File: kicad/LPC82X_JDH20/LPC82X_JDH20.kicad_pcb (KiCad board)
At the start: 2 copper layers, 18.7 x 23.8 mm, 24 parts, among them J1 Conn_01x09, J2 JTAG_2X05, J3 Conn_01x09, U1 LPC824M201JDH20, Y1 12MHz

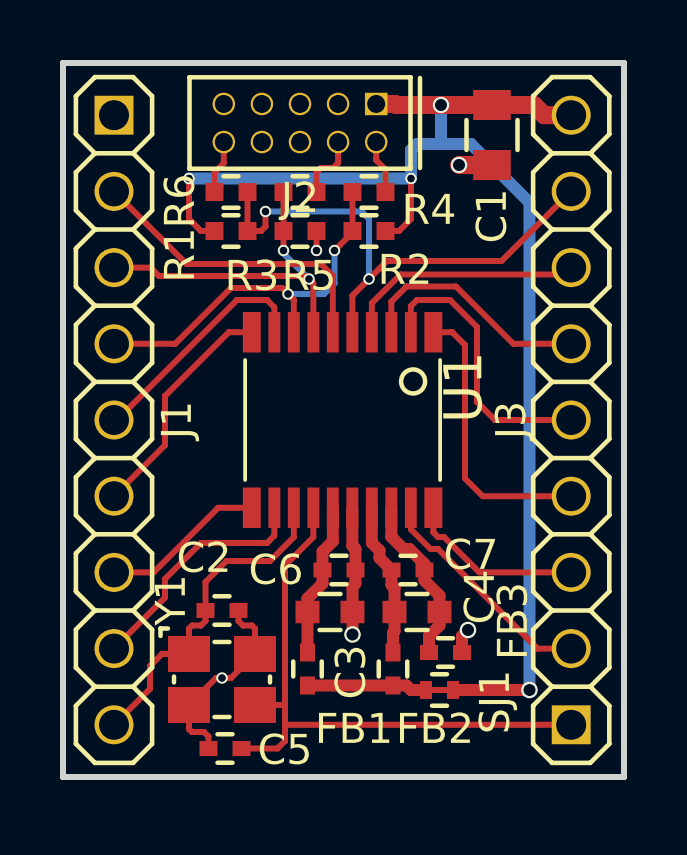
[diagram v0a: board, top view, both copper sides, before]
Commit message: updated a few traces and silk screen bits
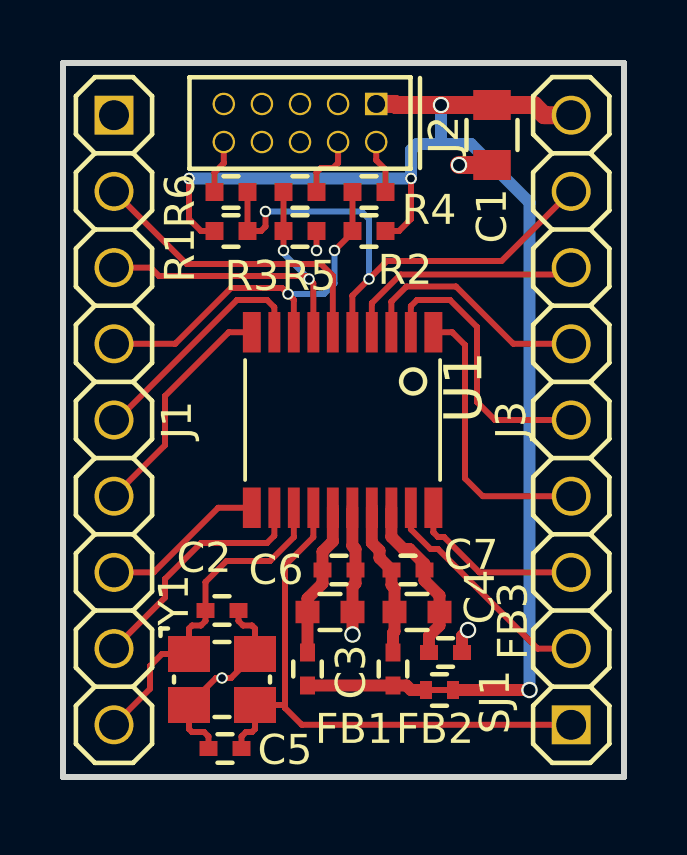
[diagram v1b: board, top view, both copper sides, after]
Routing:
- net /PIO0_8: track 20.3 -> 19.6 mm
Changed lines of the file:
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@@
     (thickness 1.6)
     (drawings 5)
-    (tracks 219)
+    (tracks 221)
     (zones 0)
     (modules 24)
@@
     (visible_elements FFFFFF7F)
     (pcbplotparams
-      (layerselection 0x00030_80000001)
-      (usegerberextensions false)
+      (layerselection 0x010f0_ffffffff)
+      (usegerberextensions true)
       (usegerberattributes false)
       (usegerberadvancedattributes false)
@@
       (outputformat 1)
       (mirror false)
-      (drillshape 1)
+      (drillshape 0)
       (scaleselection 1)
-      (outputdirectory ""))
+      (outputdirectory "LPC82X_JDH20_plots"))
   )
   (net 0 "")
@@
   (module SquantorConnectors:Header-0127-2X05-H006 (layer F.Cu)
     (at 133.2 91.7 180)
-    (fp_text reference J2 (at 0 -2.5 180) (layer F.SilkS)
+    (fp_text reference J2 (at -4.8 -0.4 270) (layer F.SilkS)
       (effects (font (size 1 1) (thickness 0.15)))
     )
@@
     (at 130.6 110.25)
     (attr smd)
-    (fp_text reference Y1 (at -1.7 -2.65 90) (layer F.SilkS)
+    (fp_text reference Y1 (at -1.6 -2.65 90) (layer F.SilkS)
       (effects (font (size 1 1) (thickness 0.15)))
     )
@@
   (segment (start 133.645 104.525) (end 133.645 105.505) (width 0.2) (layer F.Cu) (net 7))
   (segment (start 133.645 105.505) (end 132.7 106.45) (width 0.2) (layer F.Cu) (net 7))
-  (segment (start 132.45 112.55) (end 131.25 112.55) (width 0.2) (layer F.Cu) (net 7))
-  (segment (start 132.7 112.3) (end 132.45 112.55) (width 0.2) (layer F.Cu) (net 7))
-  (segment (start 132.71 111.76) (end 132.7 111.75) (width 0.2) (layer F.Cu) (net 7))
-  (segment (start 142.24 111.76) (end 132.71 111.76) (width 0.2) (layer F.Cu) (net 7))
-  (segment (start 132.7 111.75) (end 132.7 112.3) (width 0.2) (layer F.Cu) (net 7))
   (segment (start 132.65 111.1) (end 132.7 111.15) (width 0.2) (layer F.Cu) (net 7))
   (segment (start 131.7 111.1) (end 132.65 111.1) (width 0.2) (layer F.Cu) (net 7))
   (segment (start 132.7 106.45) (end 132.7 111.15) (width 0.2) (layer F.Cu) (net 7))
-  (segment (start 132.7 111.15) (end 132.7 111.75) (width 0.2) (layer F.Cu) (net 7))
+  (segment (start 131.25 112.55) (end 131.25 112.15) (width 0.2) (layer F.Cu) (net 7))
+  (segment (start 131.25 112.15) (end 131.4 112) (width 0.2) (layer F.Cu) (net 7))
+  (segment (start 131.4 112) (end 131.6 112) (width 0.2) (layer F.Cu) (net 7))
+  (segment (start 131.7 111.9) (end 131.7 111.1) (width 0.2) (layer F.Cu) (net 7))
+  (segment (start 131.6 112) (end 131.7 111.9) (width 0.2) (layer F.Cu) (net 7))
+  (segment (start 132.7 111.2) (end 132.7 111.15) (width 0.2) (layer F.Cu) (net 7))
+  (segment (start 142.24 111.76) (end 133.26 111.76) (width 0.2) (layer F.Cu) (net 7))
+  (segment (start 133.26 111.76) (end 132.7 111.2) (width 0.2) (layer F.Cu) (net 7))
   (segment (start 133.45 110.45) (end 136.3 110.45) (width 0.4) (layer F.Cu) (net 8))
   (segment (start 136.3 110.45) (end 136.75 110.45) (width 0.4) (layer F.Cu) (net 8))

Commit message: updated PCB and plots
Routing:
- net /PIO0_23: track 9.47 -> 7.74 mm
- net /PIO0_17: track 9.42 -> 7.96 mm
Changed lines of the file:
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@@
     (thickness 1.6)
     (drawings 5)
-    (tracks 221)
+    (tracks 218)
     (zones 0)
     (modules 24)
@@
     (at 134.62 101.6 180)
     (descr "<li><b>SOT360</b><hr>\n<ul><li>TSSOP20: plastic thin shrink small outline package; 20 leads; body width 4.4 mm\n<li><u>JEDEC</u>: MO-153\n<li><u>IEC</u>: </ul>")
-    (fp_text reference U1 (at -4.78 -0.1 270) (layer F.SilkS)
-      (effects (font (size 1.27 1.27) (thickness 0.15)) (justify left bottom))
-    )
-    (fp_text value LPC824M201JDH20 (at 5.3 3.6 270) (layer F.Fab)
-      (effects (font (size 1.27 1.27) (thickness 0.15)) (justify left bottom))
+    (fp_text reference U1 (at -3.5 2.2 270) (layer F.SilkS)
+      (effects (font (size 1 1) (thickness 0.15)) (justify left bottom))
+    )
+    (fp_text value LPC824M201JDH20 (at 4.6 3.1 270) (layer F.Fab)
+      (effects (font (size 1 1) (thickness 0.15)) (justify left bottom))
     )
     (fp_line (start -3.25 -2.2) (end 3.25 -2.2) (layer Dwgs.User) (width 0.127))
@@
   (segment (start 128.7 102.44) (end 127 104.14) (width 0.2) (layer F.Cu) (net 13))
   (segment (start 128.7 100.8) (end 128.7 102.44) (width 0.2) (layer F.Cu) (net 13))
-  (segment (start 131.595 104.525) (end 130.475 104.525) (width 0.2) (layer F.Cu) (net 14))
   (segment (start 128.32 106.68) (end 127 106.68) (width 0.2) (layer F.Cu) (net 14))
   (segment (start 130.475 104.525) (end 128.32 106.68) (width 0.2) (layer F.Cu) (net 14))
+  (segment (start 130.475 104.525) (end 131.595 104.525) (width 0.2) (layer F.Cu) (net 14))
   (segment (start 132.345 104.525) (end 132.345 105.455) (width 0.2) (layer F.Cu) (net 15))
   (segment (start 132.345 105.455) (end 132.1 105.7) (width 0.2) (layer F.Cu) (net 15))
@@
   (segment (start 140.31 99.06) (end 142.24 99.06) (width 0.2) (layer F.Cu) (net 21))
   (segment (start 138.4 97.15) (end 140.31 99.06) (width 0.2) (layer F.Cu) (net 21))
+  (segment (start 142.2 101.6) (end 142.24 101.6) (width 0.2) (layer F.Cu) (net 22))
+  (segment (start 138.2 97.6) (end 142.2 101.6) (width 0.2) (layer F.Cu) (net 22))
   (segment (start 136.895 98.675) (end 136.895 97.805) (width 0.2) (layer F.Cu) (net 22))
+  (segment (start 137.1 97.6) (end 138.2 97.6) (width 0.2) (layer F.Cu) (net 22))
   (segment (start 136.895 97.805) (end 137.1 97.6) (width 0.2) (layer F.Cu) (net 22))
-  (segment (start 137.1 97.6) (end 138.2 97.6) (width 0.2) (layer F.Cu) (net 22))
-  (segment (start 138.2 97.6) (end 139.1 98.5) (width 0.2) (layer F.Cu) (net 22))
-  (segment (start 139.1 98.5) (end 139.1 101) (width 0.2) (layer F.Cu) (net 22))
-  (segment (start 139.7 101.6) (end 142.24 101.6) (width 0.2) (layer F.Cu) (net 22))
-  (segment (start 139.1 101) (end 139.7 101.6) (width 0.2) (layer F.Cu) (net 22))
+  (segment (start 138.7 100.6) (end 142.24 104.14) (width 0.2) (layer F.Cu) (net 23))
+  (segment (start 138.7 99.1) (end 138.7 100.6) (width 0.2) (layer F.Cu) (net 23))
   (segment (start 137.645 98.675) (end 138.275 98.675) (width 0.2) (layer F.Cu) (net 23))
   (segment (start 138.275 98.675) (end 138.7 99.1) (width 0.2) (layer F.Cu) (net 23))
-  (segment (start 138.7 99.1) (end 138.7 103.55) (width 0.2) (layer F.Cu) (net 23))
-  (segment (start 139.29 104.14) (end 142.24 104.14) (width 0.2) (layer F.Cu) (net 23))
-  (segment (start 138.7 103.55) (end 139.29 104.14) (width 0.2) (layer F.Cu) (net 23))
   (segment (start 137.645 104.525) (end 137.645 105.345) (width 0.2) (layer F.Cu) (net 24))
   (segment (start 137.645 105.345) (end 137.8 105.5) (width 0.2) (layer F.Cu) (net 24))

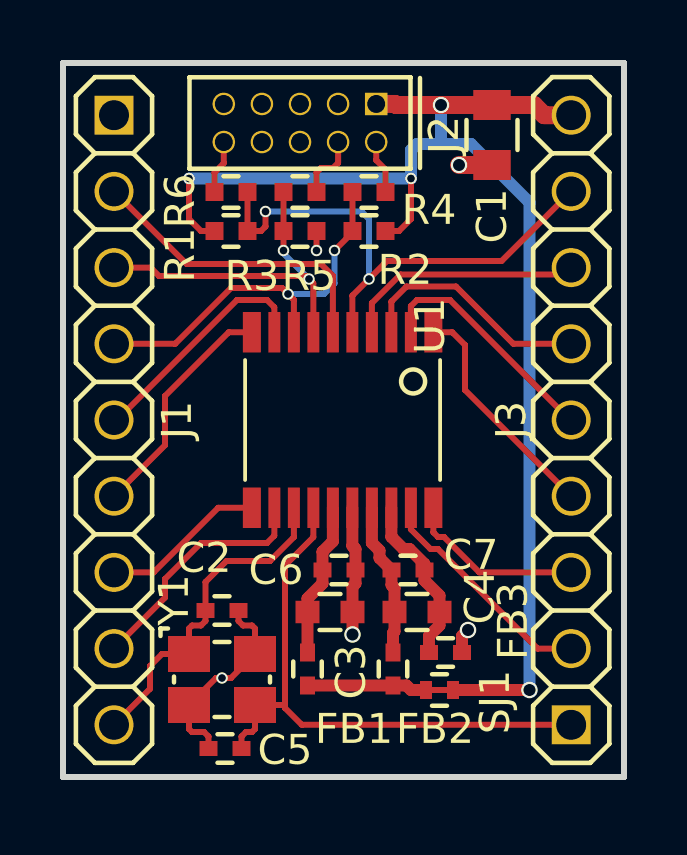
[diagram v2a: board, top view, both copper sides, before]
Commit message: small silk updates, updated values, top groundplane
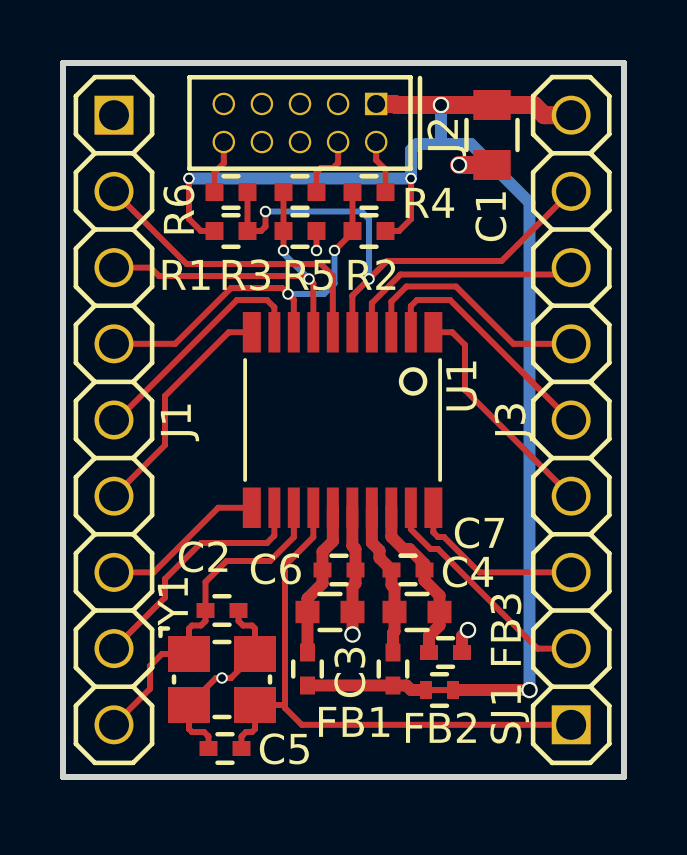
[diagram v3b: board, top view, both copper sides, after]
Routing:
- added copper zone on F.Cu, net VSS
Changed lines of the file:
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@@
     (47 F.CrtYd user)
     (48 B.Fab user)
-    (49 F.Fab user hide)
+    (49 F.Fab user)
   )
   (setup
-    (last_trace_width 0.2)
+    (last_trace_width 0.1524)
     (user_trace_width 0.1524)
     (user_trace_width 0.2)
@@
       (effects (font (size 1 1) (thickness 0.15)))
     )
-    (fp_text value 10u (at 0 2.1 90) (layer F.Fab)
+    (fp_text value 10u (at -2.7 0 90) (layer F.Fab)
       (effects (font (size 1 1) (thickness 0.15)))
     )
@@
       (effects (font (size 1 1) (thickness 0.15)))
     )
-    (fp_text value 18p (at 0 1.7) (layer F.Fab)
+    (fp_text value 18p (at -0.6 -1.75) (layer F.Fab)
       (effects (font (size 1 1) (thickness 0.15)))
     )
@@
       (effects (font (size 1 1) (thickness 0.15)))
     )
-    (fp_text value 1u (at 0 1.9) (layer F.Fab)
+    (fp_text value 1u (at 0.6 2 90) (layer F.Fab)
       (effects (font (size 1 1) (thickness 0.15)))
     )
@@
     (tags "capacitor 0603")
     (attr smd)
-    (fp_text reference C4 (at 2.1 -0.5 90) (layer F.SilkS)
-      (effects (font (size 1 1) (thickness 0.15)))
-    )
-    (fp_text value 1u (at 0 1.9) (layer F.Fab)
+    (fp_text reference C4 (at 1.7 -1.3) (layer F.SilkS)
+      (effects (font (size 1 1) (thickness 0.15)))
+    )
+    (fp_text value 1u (at 1.8 -1.4) (layer F.Fab)
       (effects (font (size 1 1) (thickness 0.15)))
     )
@@
       (effects (font (size 1 1) (thickness 0.15)))
     )
-    (fp_text value 18p (at 0 1.7 180) (layer F.Fab)
+    (fp_text value 18p (at -2 -0.05 180) (layer F.Fab)
       (effects (font (size 1 1) (thickness 0.15)))
     )
@@
       (effects (font (size 1 1) (thickness 0.15)))
     )
-    (fp_text value 100n (at 0 1.7) (layer F.Fab)
+    (fp_text value 100n (at -2 0) (layer F.Fab)
       (effects (font (size 1 1) (thickness 0.15)))
     )
@@
     (tags "capacitor 0402")
     (attr smd)
-    (fp_text reference C7 (at 2.1 -0.5) (layer F.SilkS)
-      (effects (font (size 1 1) (thickness 0.15)))
-    )
-    (fp_text value 100n (at 0 1.7) (layer F.Fab)
+    (fp_text reference C7 (at 2.4 -1.2) (layer F.SilkS)
+      (effects (font (size 1 1) (thickness 0.15)))
+    )
+    (fp_text value 100n (at 2.5 -1.2) (layer F.Fab)
       (effects (font (size 1 1) (thickness 0.15)))
     )
@@
     (tags "capacitor 0402")
     (attr smd)
-    (fp_text reference FB1 (at 2 -1.55 180) (layer F.SilkS)
-      (effects (font (size 1 1) (thickness 0.15)))
-    )
-    (fp_text value FB (at 0 1.7 270) (layer F.Fab)
+    (fp_text reference FB1 (at 1.8 -1.55 180) (layer F.SilkS)
+      (effects (font (size 1 1) (thickness 0.15)))
+    )
+    (fp_text value FB (at 1.8 -1.55 180) (layer F.Fab)
       (effects (font (size 1 1) (thickness 0.15)))
     )
@@
     (tags "capacitor 0402")
     (attr smd)
-    (fp_text reference FB2 (at 2 -1.4 180) (layer F.SilkS)
-      (effects (font (size 1 1) (thickness 0.15)))
-    )
-    (fp_text value FB (at 0 1.7 270) (layer F.Fab)
+    (fp_text reference FB2 (at 2 -1.6 180) (layer F.SilkS)
+      (effects (font (size 1 1) (thickness 0.15)))
+    )
+    (fp_text value FB (at 2 -1.6 180) (layer F.Fab)
       (effects (font (size 1 1) (thickness 0.15)))
     )
@@
     (tags "capacitor 0402")
     (attr smd)
-    (fp_text reference FB3 (at 2.25 -1.05 90) (layer F.SilkS)
-      (effects (font (size 1 1) (thickness 0.15)))
-    )
-    (fp_text value FB (at 0 1.7) (layer F.Fab)
+    (fp_text reference FB3 (at 2.05 -0.75 90) (layer F.SilkS)
+      (effects (font (size 1 1) (thickness 0.15)))
+    )
+    (fp_text value FB (at 2.05 -0.95 90) (layer F.Fab)
       (effects (font (size 1 1) (thickness 0.15)))
     )
@@
     (tags "resistor 0402")
     (attr smd)
-    (fp_text reference R1 (at -1.7 0.8 90) (layer F.SilkS)
-      (effects (font (size 1 1) (thickness 0.15)))
-    )
-    (fp_text value 100K (at 0 1.8) (layer F.Fab)
+    (fp_text reference R1 (at -1.5 1.5) (layer F.SilkS)
+      (effects (font (size 1 1) (thickness 0.15)))
+    )
+    (fp_text value 100K (at -1.6 1.5) (layer F.Fab)
       (effects (font (size 1 1) (thickness 0.15)))
     )
@@
     (tags "resistor 0402")
     (attr smd)
-    (fp_text reference R2 (at -1.2 -1.3 180) (layer F.SilkS)
-      (effects (font (size 1 1) (thickness 0.15)))
-    )
-    (fp_text value 100k (at 0 1.8 180) (layer F.Fab)
+    (fp_text reference R2 (at -0.1 -1.5 180) (layer F.SilkS)
+      (effects (font (size 1 1) (thickness 0.15)))
+    )
+    (fp_text value 100k (at -0.6 -1.6 180) (layer F.Fab)
       (effects (font (size 1 1) (thickness 0.15)))
     )
@@
     (tags "resistor 0402")
     (attr smd)
-    (fp_text reference R3 (at 1.6 -1.5 180) (layer F.SilkS)
-      (effects (font (size 1 1) (thickness 0.15)))
-    )
-    (fp_text value 100k (at 0 1.8 180) (layer F.Fab)
+    (fp_text reference R3 (at 1.8 -1.5 180) (layer F.SilkS)
+      (effects (font (size 1 1) (thickness 0.15)))
+    )
+    (fp_text value 100k (at 1.6 -1.5 180) (layer F.Fab)
       (effects (font (size 1 1) (thickness 0.15)))
     )
@@
     (tags "resistor 0402")
     (attr smd)
-    (fp_text reference R4 (at -2 -0.6 180) (layer F.SilkS)
-      (effects (font (size 1 1) (thickness 0.15)))
-    )
-    (fp_text value 100 (at 0 1.8 180) (layer F.Fab)
+    (fp_text reference R4 (at -2 -0.4 180) (layer F.SilkS)
+      (effects (font (size 1 1) (thickness 0.15)))
+    )
+    (fp_text value 100 (at -2.2 -0.5 180) (layer F.Fab)
       (effects (font (size 1 1) (thickness 0.15)))
     )
@@
       (effects (font (size 1 1) (thickness 0.15)))
     )
-    (fp_text value 100 (at 0 1.8 180) (layer F.Fab)
+    (fp_text value 100 (at -0.5 -2.8 180) (layer F.Fab)
       (effects (font (size 1 1) (thickness 0.15)))
     )
@@
     (tags "resistor 0402")
     (attr smd)
-    (fp_text reference R6 (at -1.7 0.3 90) (layer F.SilkS)
-      (effects (font (size 1 1) (thickness 0.15)))
-    )
-    (fp_text value 100 (at 0 1.8) (layer F.Fab)
+    (fp_text reference R6 (at -1.7 0.6 90) (layer F.SilkS)
+      (effects (font (size 1 1) (thickness 0.15)))
+    )
+    (fp_text value 100 (at -1.7 0.6 90) (layer F.Fab)
       (effects (font (size 1 1) (thickness 0.15)))
     )
@@
     (tags "resistor 0402")
     (attr smd)
-    (fp_text reference SJ1 (at -1.85 -0.4 270) (layer F.SilkS)
+    (fp_text reference SJ1 (at -2.25 -0.8 270) (layer F.SilkS)
       (effects (font (size 1 1) (thickness 0.15)))
     )
@@
       (effects (font (size 1 1) (thickness 0.15)))
     )
-    (fp_text value 12MHz (at 0 2.5) (layer F.Fab)
+    (fp_text value 12MHz (at -1.7 -4.15 90) (layer F.Fab)
       (effects (font (size 1 1) (thickness 0.15)))
     )
@@
     (at 134.62 101.6 180)
     (descr "<li><b>SOT360</b><hr>\n<ul><li>TSSOP20: plastic thin shrink small outline package; 20 leads; body width 4.4 mm\n<li><u>JEDEC</u>: MO-153\n<li><u>IEC</u>: </ul>")
-    (fp_text reference U1 (at -3.5 2.2 270) (layer F.SilkS)
+    (fp_text reference U1 (at -4.58 0.2 270) (layer F.SilkS)
       (effects (font (size 1 1) (thickness 0.15)) (justify left bottom))
     )
-    (fp_text value LPC824M201JDH20 (at 4.6 3.1 270) (layer F.Fab)
+    (fp_text value LPC824M201JDH20 (at 4.6 3.1 270) (layer F.Fab) hide
       (effects (font (size 1 1) (thickness 0.15)) (justify left bottom))
     )
@@
     (fill yes (arc_segments 16) (thermal_gap 0.508) (thermal_bridge_width 0.508))
     (polygon
+      (pts
+        (xy 125.3 89.7) (xy 144 89.7) (xy 144 113.5) (xy 125.3 113.5)
+      )
+    )
+  )
+  (zone (net 1) (net_name VSS) (layer F.Cu) (hatch edge 0.508)
+    (connect_pads (clearance 0.3))
+    (min_thickness 0.254)
+    (fill yes (arc_segments 16) (thermal_gap 0.508) (thermal_bridge_width 0.508))
+    (polygon

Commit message: fixed incorrect crystal footprint and relayout
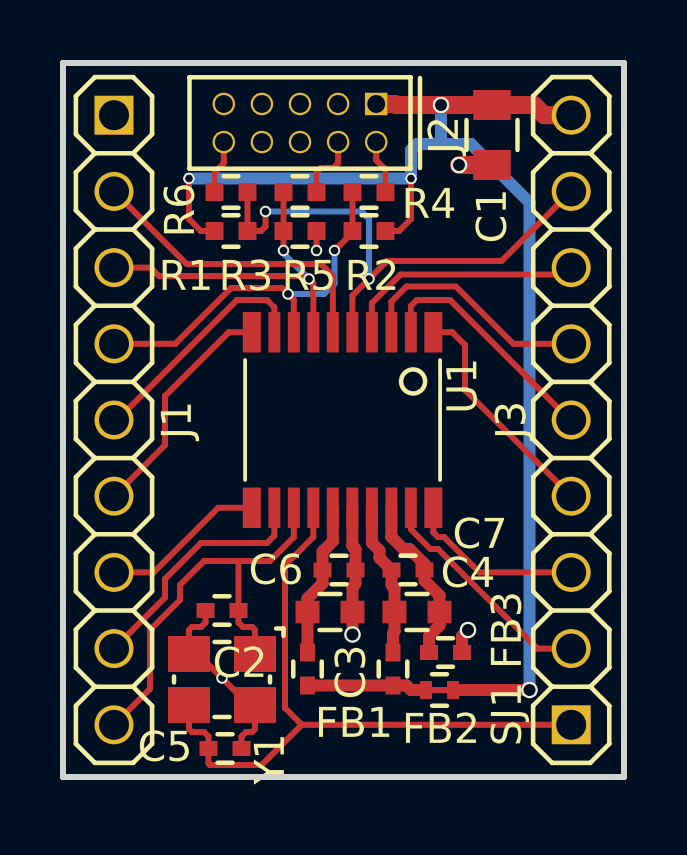
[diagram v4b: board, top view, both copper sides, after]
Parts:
- turned C2 to 180 degrees
- turned C5 to 0 degrees
- turned Y1 to 180 degrees
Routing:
- net /PIO0_8: track 19.6 -> 23.0 mm
- net /PIO0_9: track 11.3 -> 14.5 mm
